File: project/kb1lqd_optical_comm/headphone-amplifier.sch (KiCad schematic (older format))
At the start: 12 parts, among them U4 TPA6111A2D

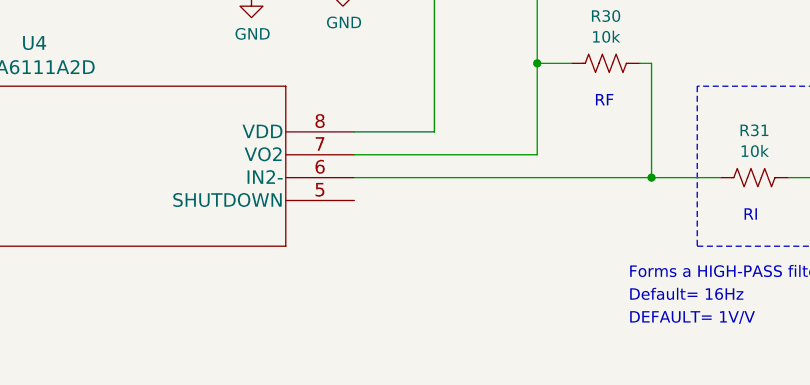
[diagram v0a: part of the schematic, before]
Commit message: Fixing ERC errors.
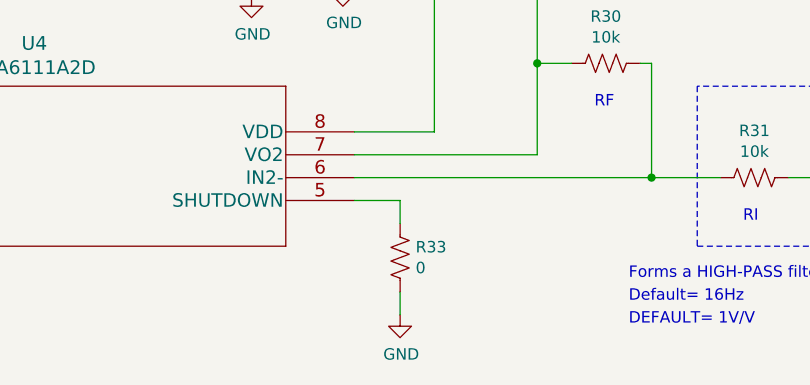
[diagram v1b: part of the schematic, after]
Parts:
- added R33: 0, symbol Device:R_US
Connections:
- net GND: now also R33.1
- net at U4.5 (SHUTDOWN): now also R33.2
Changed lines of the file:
@@
 Text Notes 7750 4250 0    50   ~ 0
 DEFAULT= 1V/V
+$Comp
+L Device:R_US R33
+U 1 1 5FE8B5BB
+P 6750 3950
+F 0 "R33" H 6682 3904 50  0000 R CNN
+F 1 "0" H 6682 3995 50  0000 R CNN
+F 2 "" V 6790 3940 50  0001 C CNN
+F 3 "~" H 6750 3950 50  0001 C CNN
+	1    6750 3950
+	-1   0    0    1
+$EndComp
+Wire Wire Line
+	6550 3700 6750 3700
+Wire Wire Line
+	6750 3700 6750 3800
+$Comp
+L power:GND #PWR0106
+U 1 1 5FE8D8D8
+P 6750 4200
+F 0 "#PWR0106" H 6750 3950 50  0001 C CNN
+F 1 "GND" H 6755 4027 50  0000 C CNN
+F 2 "" H 6750 4200 50  0001 C CNN
+F 3 "" H 6750 4200 50  0001 C CNN
+	1    6750 4200
+	1    0    0    -1
+$EndComp
+Wire Wire Line
+	6750 4200 6750 4100
 $EndSCHEMATC

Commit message: Updated with all footprints
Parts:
- removed C16: 10uF, symbol Device:C
- added C16: 10uF, Capacitor_SMD:CP_Elec_5x5.3, symbol Device:CP1
- C13, C14, C15, C18, C19: footprint (none) -> Capacitor_SMD:C_1206_3216Metric
- C17: footprint (none) -> Capacitor_SMD:C_0805_2012Metric
- R28, R29, R30, R31, R33: footprint (none) -> Resistor_SMD:R_0603_1608Metric
- U4: footprint D8 -> TPA6111A2D:TPA6111A2D
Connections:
- net +5V: now also C16.1
- net GND: now also C16.2
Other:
- note added: "UWR1H100MCL1GB"
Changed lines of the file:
@@
 F 0 "U4" H 5150 3787 60  0000 C CNN
 F 1 "TPA6111A2D" H 5150 3681 60  0000 C CNN
-F 2 "D8" H 5150 3640 60  0001 C CNN
+F 2 "TPA6111A2D:TPA6111A2D" H 5150 3640 60  0001 C CNN
 F 3 "" H 3750 3400 60  0000 C CNN
 	1    3750 3400
@@
 F 0 "R28" V 2195 3500 50  0000 C CNN
 F 1 "10k" V 2286 3500 50  0000 C CNN
-F 2 "" V 2440 3490 50  0001 C CNN
+F 2 "Resistor_SMD:R_0603_1608Metric" V 2440 3490 50  0001 C CNN
 F 3 "~" H 2400 3500 50  0001 C CNN
 	1    2400 3500
@@
 F 0 "C15" H 3285 2354 50  0000 R CNN
 F 1 "1uF" H 3285 2445 50  0000 R CNN
-F 2 "" H 3438 2250 50  0001 C CNN
+F 2 "Capacitor_SMD:C_1206_3216Metric" H 3438 2250 50  0001 C CNN
 F 3 "~" H 3400 2400 50  0001 C CNN
 	1    3400 2400
@@
 F 0 "R29" V 2945 3100 50  0000 C CNN
 F 1 "10k" V 3036 3100 50  0000 C CNN
-F 2 "" V 3190 3090 50  0001 C CNN
+F 2 "Resistor_SMD:R_0603_1608Metric" V 3190 3090 50  0001 C CNN
 F 3 "~" H 3150 3100 50  0001 C CNN
 	1    3150 3100
@@
 F 0 "R31" V 8095 3600 50  0000 C CNN
 F 1 "10k" V 8186 3600 50  0000 C CNN
-F 2 "" V 8340 3590 50  0001 C CNN
+F 2 "Resistor_SMD:R_0603_1608Metric" V 8340 3590 50  0001 C CNN
 F 3 "~" H 8300 3600 50  0001 C CNN
 	1    8300 3600
@@
 F 0 "C18" H 7235 2354 50  0000 R CNN
 F 1 "1uF" H 7235 2445 50  0000 R CNN
-F 2 "" H 7388 2250 50  0001 C CNN
+F 2 "Capacitor_SMD:C_1206_3216Metric" H 7388 2250 50  0001 C CNN
 F 3 "~" H 7350 2400 50  0001 C CNN
 	1    7350 2400
@@
 F 0 "R30" V 7445 3100 50  0000 C CNN
 F 1 "10k" V 7536 3100 50  0000 C CNN
-F 2 "" V 7690 3090 50  0001 C CNN
+F 2 "Resistor_SMD:R_0603_1608Metric" V 7690 3090 50  0001 C CNN
 F 3 "~" H 7650 3100 50  0001 C CNN
 	1    7650 3100
@@
 F 0 "C13" V 2052 3500 50  0000 C CNN
 F 1 "1uF" V 1961 3500 50  0000 C CNN
-F 2 "" H 1838 3350 50  0001 C CNN
+F 2 "Capacitor_SMD:C_1206_3216Metric" H 1838 3350 50  0001 C CNN
 F 3 "~" H 1800 3500 50  0001 C CNN
 	1    1800 3500
@@
 F 0 "C19" V 8952 3600 50  0000 C CNN
 F 1 "1uF" V 8861 3600 50  0000 C CNN
-F 2 "" H 8738 3450 50  0001 C CNN
+F 2 "Capacitor_SMD:C_1206_3216Metric" H 8738 3450 50  0001 C CNN
 F 3 "~" H 8700 3600 50  0001 C CNN
 	1    8700 3600
@@
 F 0 "C17" H 6385 2404 50  0000 R CNN
 F 1 "100nF" H 6385 2495 50  0000 R CNN
-F 2 "" H 6538 2300 50  0001 C CNN
+F 2 "Capacitor_SMD:C_0805_2012Metric" H 6538 2300 50  0001 C CNN
 F 3 "~" H 6500 2450 50  0001 C CNN
 	1    6500 2450
@@
 F 0 "C14" H 3185 3854 50  0000 R CNN
 F 1 "1uF" H 3185 3945 50  0000 R CNN
-F 2 "" H 3338 3750 50  0001 C CNN
+F 2 "Capacitor_SMD:C_1206_3216Metric" H 3338 3750 50  0001 C CNN
 F 3 "~" H 3300 3900 50  0001 C CNN
 	1    3300 3900
@@
 	1    6100 2800
 	1    0    0    -1
-$EndComp
-$Comp
-L Device:C C16
-U 1 1 5FD9D1ED
-P 6100 2450
-F 0 "C16" H 5985 2404 50  0000 R CNN
-F 1 "10uF" H 5985 2495 50  0000 R CNN
-F 2 "" H 6138 2300 50  0001 C CNN
-F 3 "~" H 6100 2450 50  0001 C CNN
-	1    6100 2450
-	-1   0    0    1
 $EndComp
 Wire Wire Line
@@
 F 0 "R33" H 6682 3904 50  0000 R CNN
 F 1 "0" H 6682 3995 50  0000 R CNN
-F 2 "" V 6790 3940 50  0001 C CNN
+F 2 "Resistor_SMD:R_0603_1608Metric" V 6790 3940 50  0001 C CNN
 F 3 "~" H 6750 3950 50  0001 C CNN
 	1    6750 3950
@@
 Wire Wire Line
 	6750 4200 6750 4100
+$Comp
+L Device:CP1 C16
+U 1 1 5FD77F92
+P 6100 2450
+F 0 "C16" H 6215 2496 50  0000 L CNN
+F 1 "10uF" H 6215 2405 50  0000 L CNN
+F 2 "Capacitor_SMD:CP_Elec_5x5.3" H 6100 2450 50  0001 C CNN
+F 3 "~" H 6100 2450 50  0001 C CNN
+	1    6100 2450
+	1    0    0    -1
+$EndComp
+Text Notes 5600 2050 0    50   ~ 0
+UWR1H100MCL1GB
 $EndSCHEMATC
